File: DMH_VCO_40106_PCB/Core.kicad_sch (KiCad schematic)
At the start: 43 parts, among them Q1 BC558, Q2 BC548, U1 40106, U2 TL074

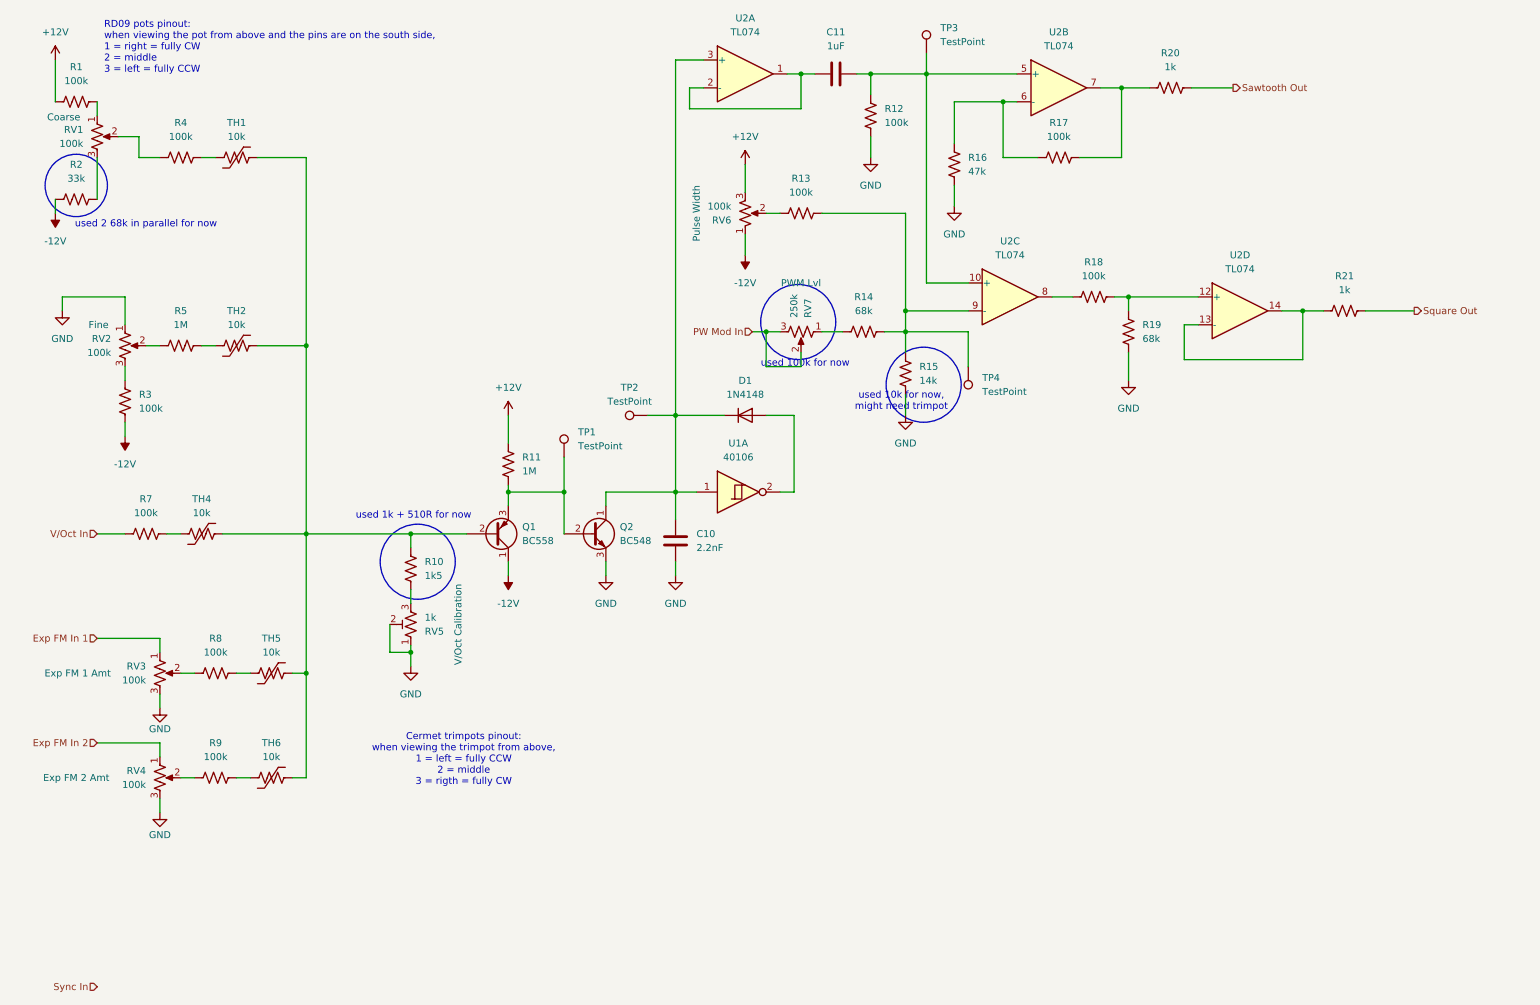
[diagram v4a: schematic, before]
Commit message: Added inverting summer to CV intake
Design not finished, needs testing and calibration
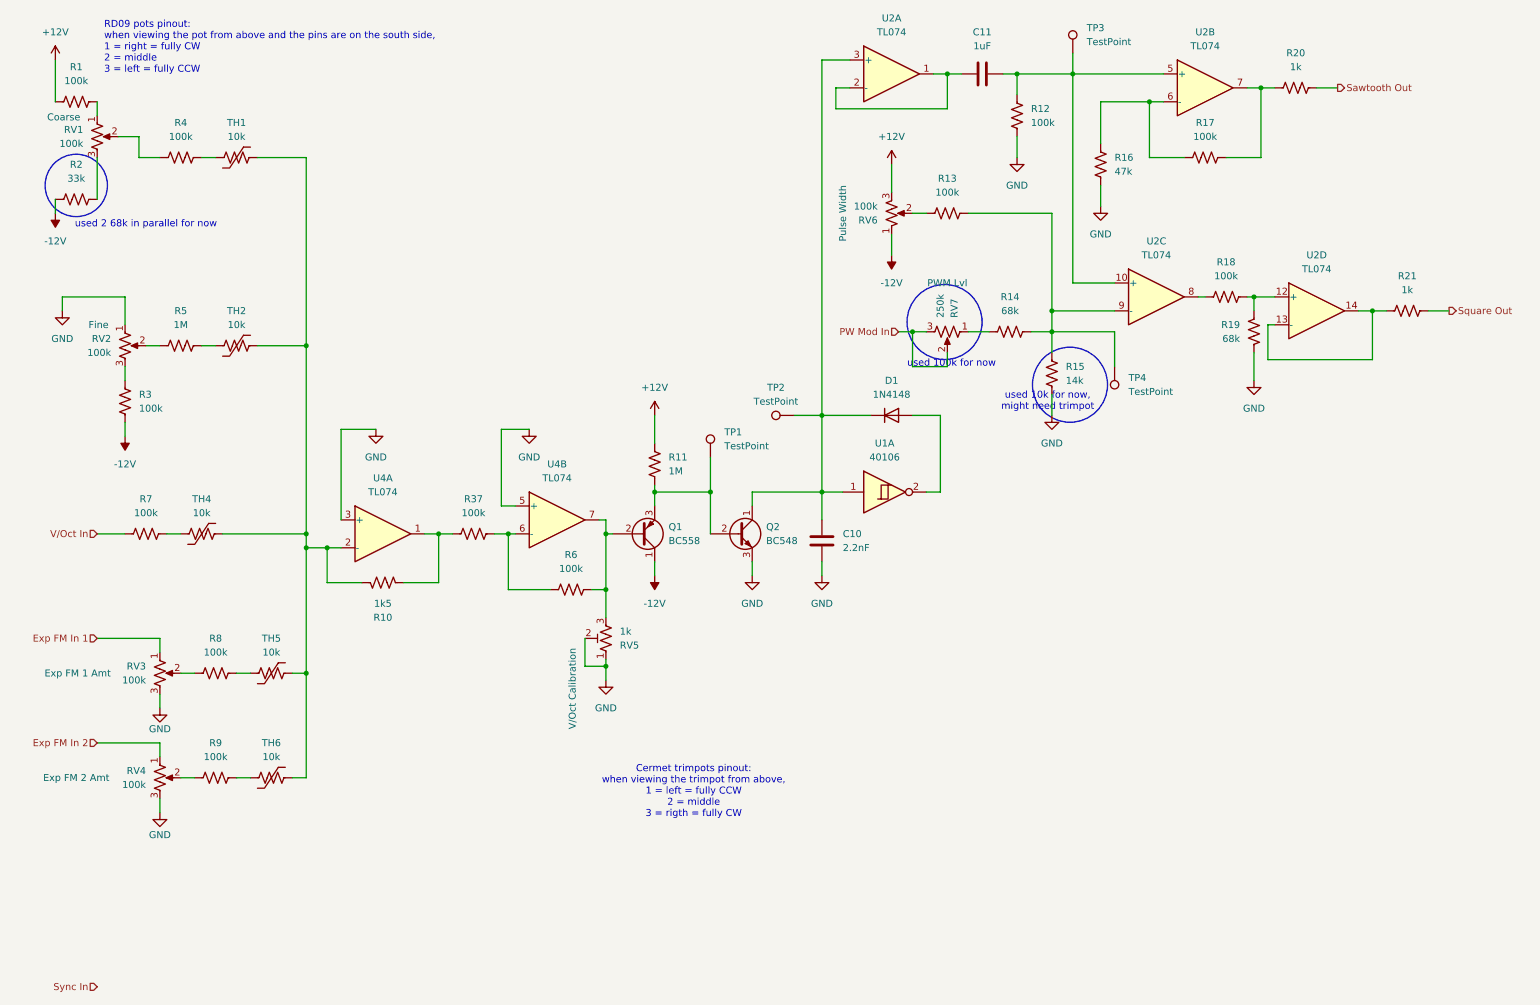
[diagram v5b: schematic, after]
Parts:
- added R37, R6: 100k, Resistor_THT:R_Axial_DIN0204_L3.6mm_D1.6mm_P5.08mm_Horizontal, symbol Device:R_US
- added U4: TL074, Package_DIP:DIP-14_W7.62mm_Socket, symbol Amplifier_Operational:TL074
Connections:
- net GND: now also U4.3 (+), U4.5 (+)
- net at TH1.2, TH2.2, TH4.2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: now also R10.1, U4.2 (-); no longer Q1.2 (B), R10.2
- net at RV5.3: now also Q1.2 (B), R6.2, U4.7; no longer R10.1
- new net: R37.2, R6.1, U4.6 (-)
- new net: R10.2, R37.1, U4.1
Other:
- note removed: "used 1k + 510R for now"
- moved on the sheet: C10, C11, D1, Q1, Q2, R10, R11, R12, R13, R14, R15, R16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

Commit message: V/Oct tracking in progress
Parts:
- added R38: 470R, Resistor_THT:R_Axial_DIN0204_L3.6mm_D1.6mm_P5.08mm_Horizontal, symbol Device:R_US
- R10: value 1k5 -> 100k
- R6: value 100k -> 1k5
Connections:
- net GND: now also R38.2; no longer RV5.1, RV5.2
- net at R6.2, U4.7: now also RV5.1; no longer Q1.2 (B), RV5.3
- new net: Q1.2 (B), RV5.2
- new net: R38.1, RV5.3
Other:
- moved on the sheet: Q1, RV5

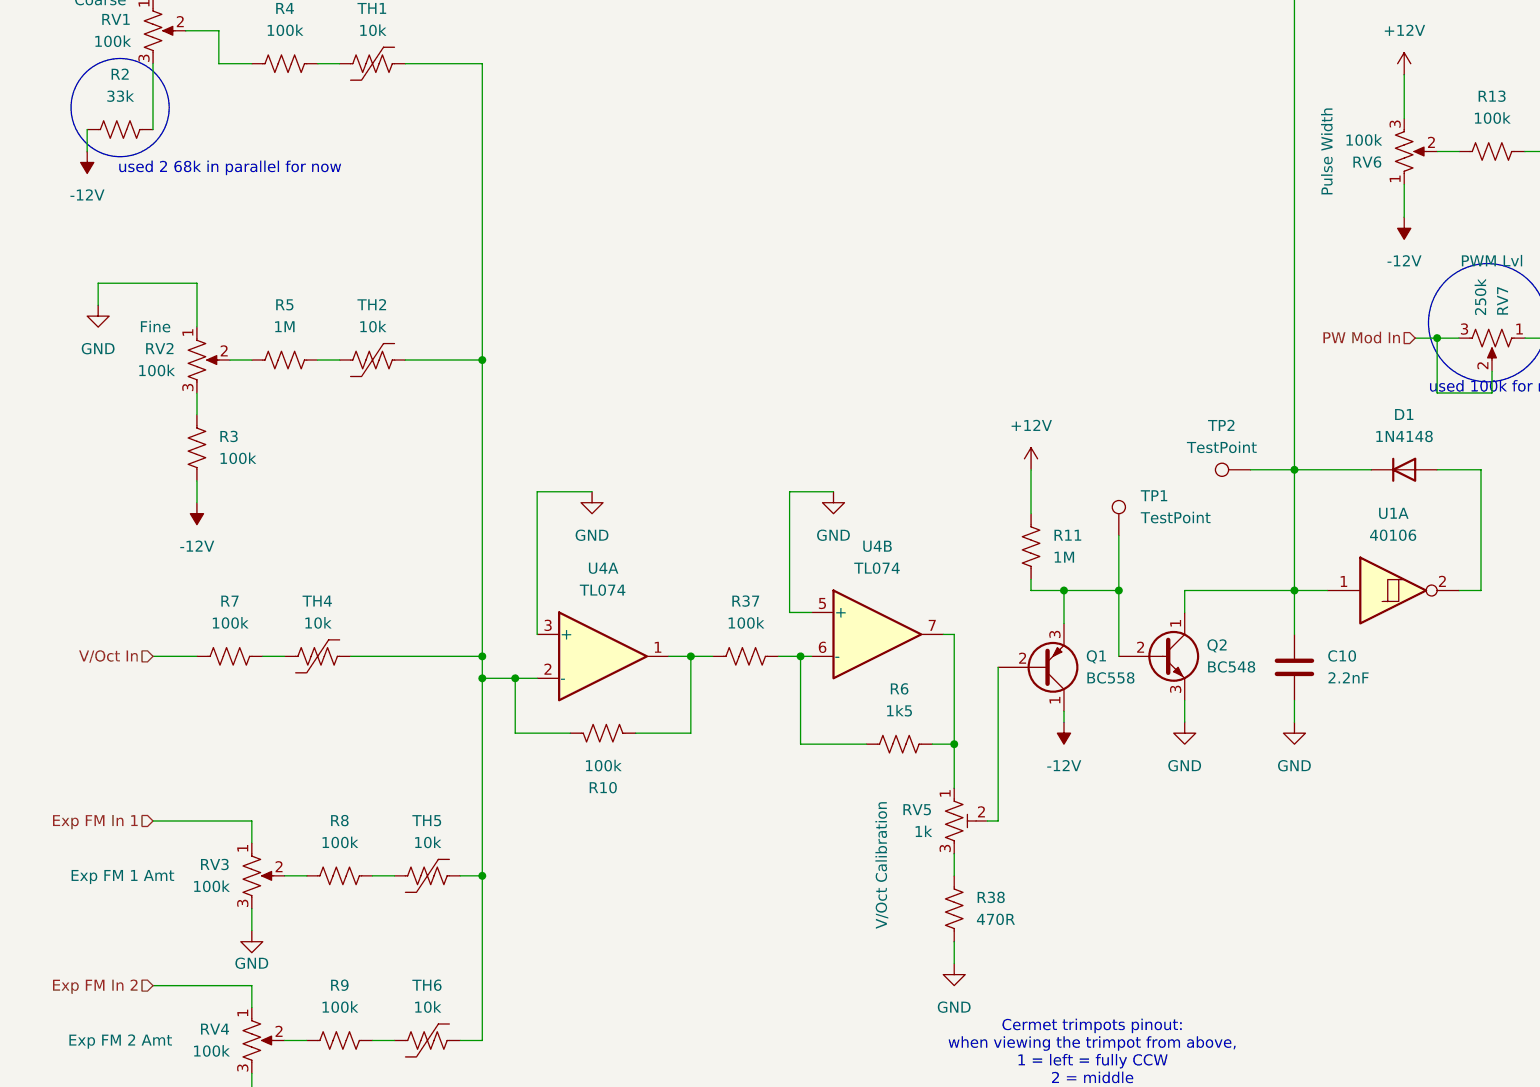
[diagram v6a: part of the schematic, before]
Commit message: Updated exponentiator resistors and capacitors
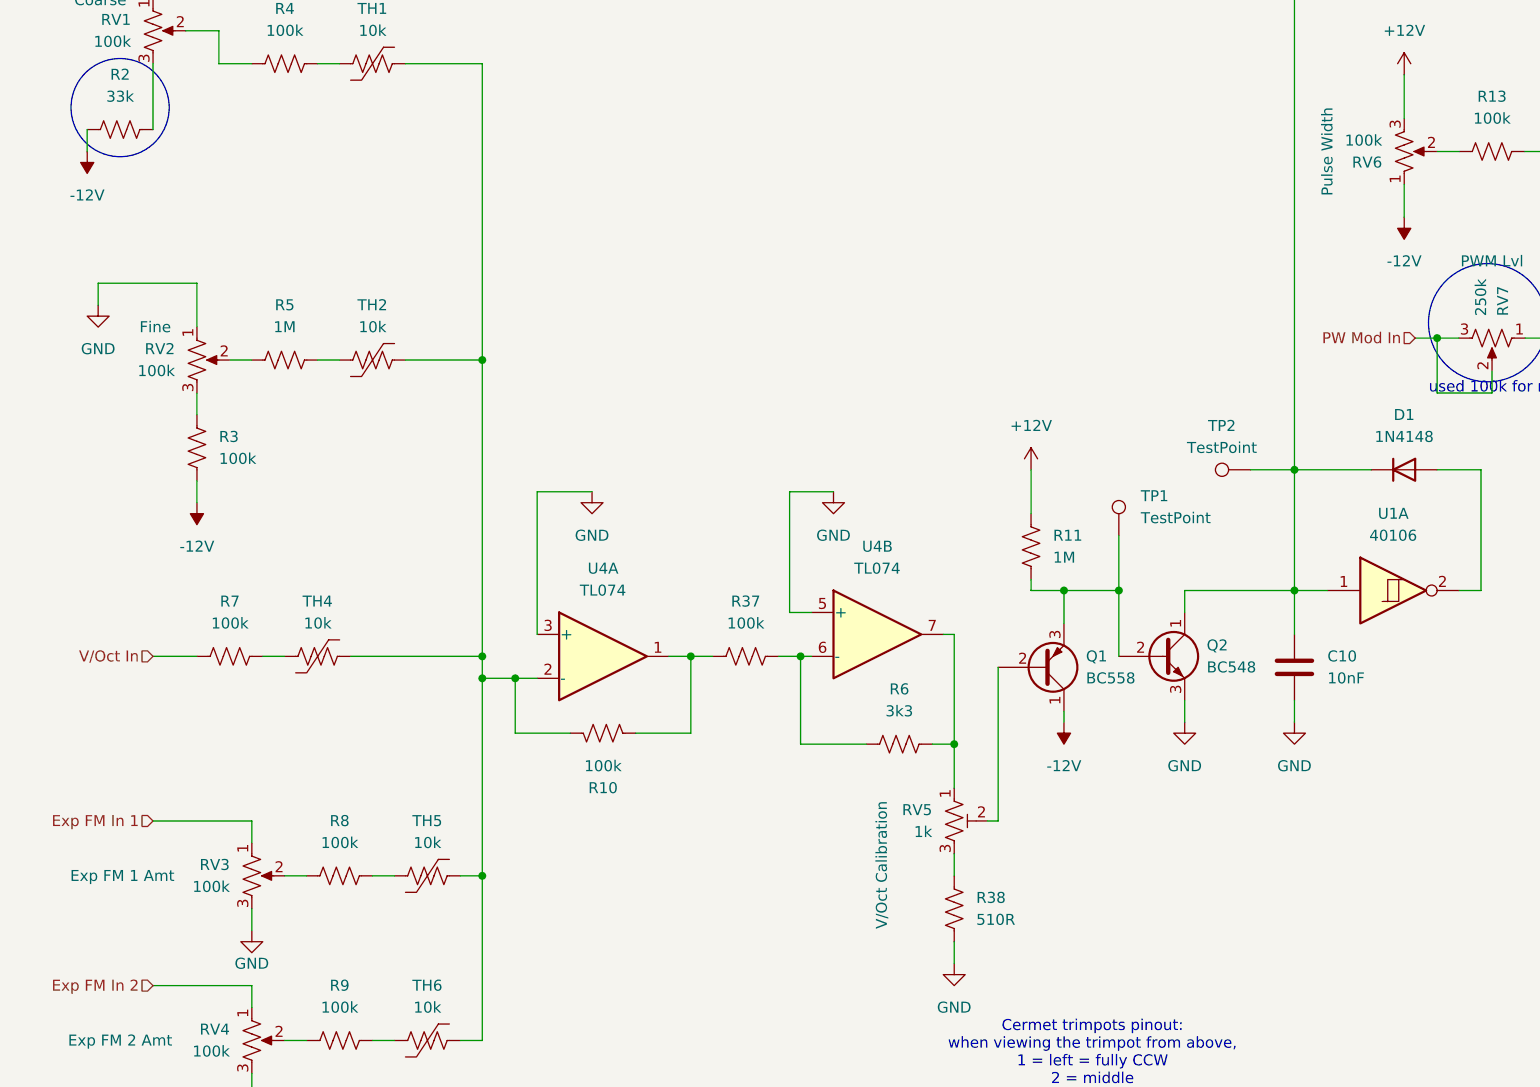
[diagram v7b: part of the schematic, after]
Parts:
- C10: value 2.2nF -> 10nF
- R38: value 470R -> 510R
- R6: value 1k5 -> 3k3
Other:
- note removed: "used 2 68k in parallel for now"
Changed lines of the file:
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@@
 		)
 	)
-	(text "used 2 68k in parallel for now"
-		(exclude_from_sim no)
-		(at 34.29 51.562 0)
-		(effects
-			(font
-				(size 1.27 1.27)
-			)
-		)
-	)
 	(hierarchical_label "Exp FM In 1"
 		(shape input)
@@
 			)
 		)
-		(property "Value" "1k5"
+		(property "Value" "3k3"
 			(at 111.76 114.3 90)
 			(effects
@@
 			)
 		)
-		(property "Value" "2.2nF"
+		(property "Value" "10nF"
 			(at 161.29 110.4899 0)
 			(effects
@@
 			)
 		)
-		(property "Value" "470R"
+		(property "Value" "510R"
 			(at 120.65 138.4299 0)
 			(effects

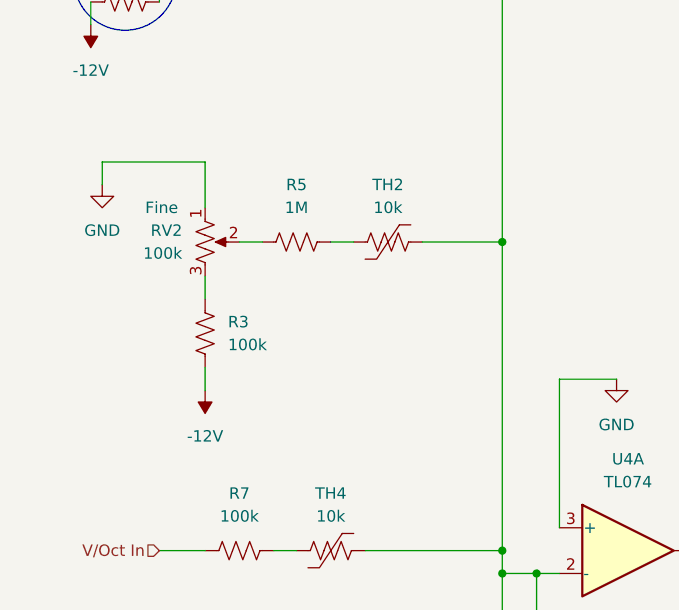
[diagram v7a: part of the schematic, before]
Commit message: Added trimpots for fine centering and range
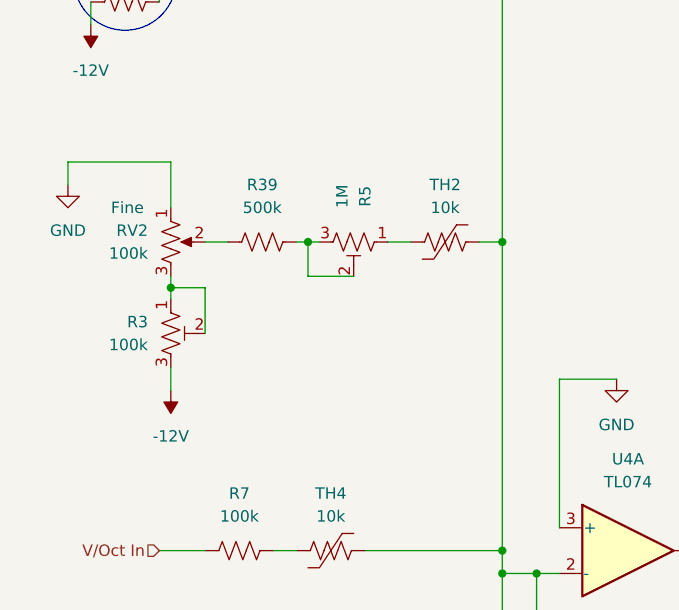
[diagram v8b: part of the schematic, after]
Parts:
- added R39: 500k, Resistor_THT:R_Axial_DIN0204_L3.6mm_D1.6mm_P5.08mm_Horizontal, symbol Device:R_US
- R3, R5: symbol Device:R_US -> Device:R_Potentiometer_Trim_US
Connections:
- net -12V: now also R3.3; no longer R3.2
- net at R5.1: now also TH2.1; no longer RV2.2
- net at R5.2: now also R5.3, R39.2; no longer TH2.1
- net at R3.1, RV2.3: now also R3.2
- new net: R39.1, RV2.2
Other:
- moved on the sheet: RV2, TH2
